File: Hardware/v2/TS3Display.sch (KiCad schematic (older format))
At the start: 28 parts, among them J1 Conn_01x05, J2 Conn_ARM_JTAG_SWD_10, SW1 SW_Push, U1 SPX3819M5-L-3-3, U2 USBLC6-2P6, U3 ATSAMD21G18A-AU, U4 NHD-2.8-240320AF-CSXP-F, U5 PAM2804, Y1 32.768k

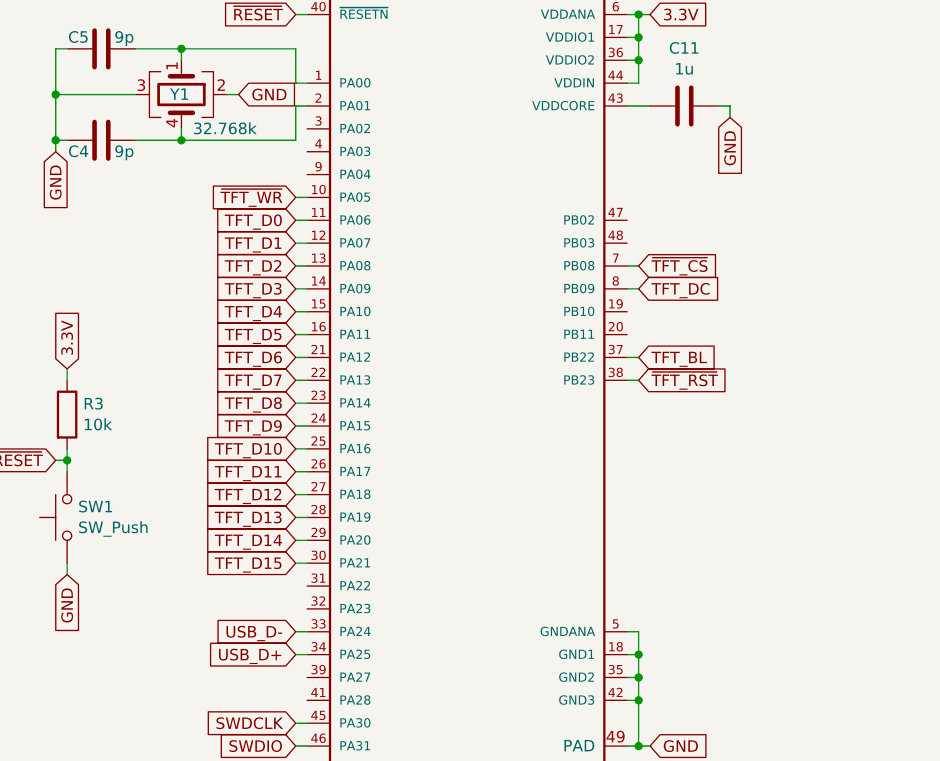
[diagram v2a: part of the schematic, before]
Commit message: Fix mirrored LCD FPC pinout
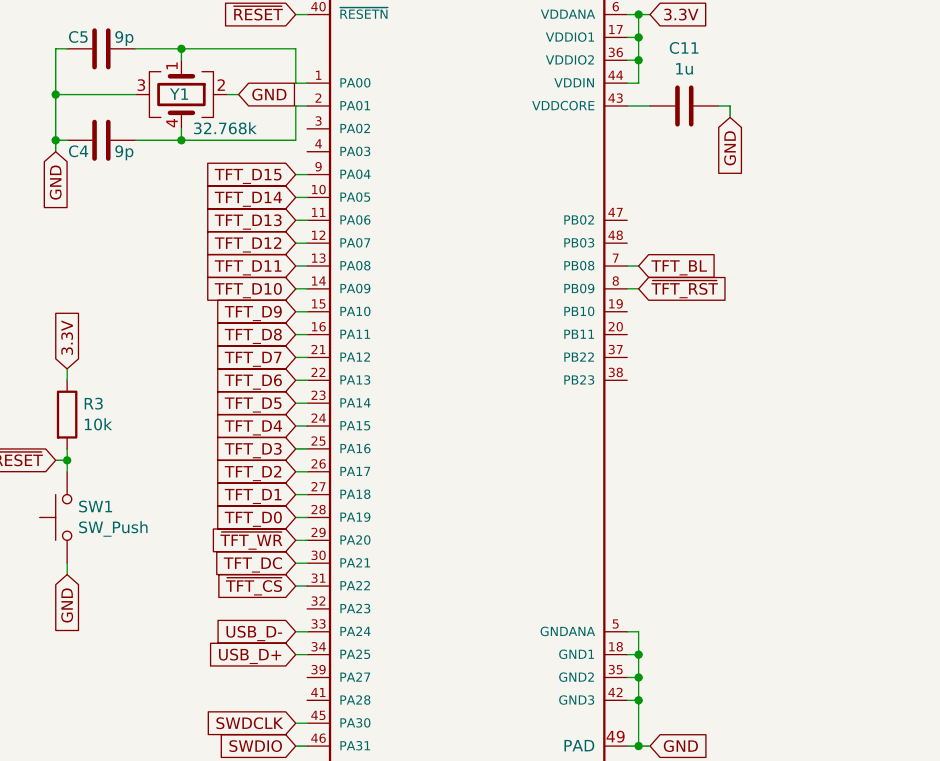
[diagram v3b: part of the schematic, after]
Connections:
- net TFT_BL: now also U3.7 (PB08); no longer U3.37 (PB22)
- net TFT_D0: now also U3.28 (PA19); no longer U3.11 (PA06)
- net TFT_D1: now also U3.27 (PA18); no longer U3.12 (PA07)
- net TFT_D10: now also U3.14 (PA09); no longer U3.25 (PA16)
- net TFT_D11: now also U3.13 (PA08); no longer U3.26 (PA17)
- net TFT_D12: now also U3.12 (PA07); no longer U3.27 (PA18)
- net TFT_D13: now also U3.11 (PA06); no longer U3.28 (PA19)
- net TFT_D14: now also U3.10 (PA05); no longer U3.29 (PA20)
- net TFT_D15: now also U3.9 (PA04); no longer U3.30 (PA21)
- net TFT_D2: now also U3.26 (PA17); no longer U3.13 (PA08)
- net TFT_D3: now also U3.25 (PA16); no longer U3.14 (PA09)
- net TFT_D4: now also U3.24 (PA15); no longer U3.15 (PA10)
- net TFT_D5: now also U3.23 (PA14); no longer U3.16 (PA11)
- net TFT_D6: now also U3.22 (PA13); no longer U3.21 (PA12)
- net TFT_D7: now also U3.21 (PA12); no longer U3.22 (PA13)
- net TFT_D8: now also U3.16 (PA11); no longer U3.23 (PA14)
- net TFT_D9: now also U3.15 (PA10); no longer U3.24 (PA15)
- net TFT_DC: now also U3.30 (PA21); no longer U3.8 (PB09)
- net ~TFT_CS: now also U3.31 (PA22); no longer U3.7 (PB08)
- net ~TFT_RST: now also U3.8 (PB09); no longer U3.38 (PB23)
- net ~TFT_WR: now also U3.29 (PA20); no longer U3.10 (PA05)
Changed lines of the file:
@@
 Wire Wire Line
 	4600 4550 4650 4550
-Wire Wire Line
-	4600 4650 4650 4650
-Wire Wire Line
-	4600 4750 4650 4750
-Text GLabel 4600 3150 0    50   Input ~ 0
-~TFT_WR
-Text GLabel 6100 3550 2    50   Input ~ 0
-TFT_DC
-Text GLabel 6100 3450 2    50   Input ~ 0
-~TFT_CS
-Text GLabel 6100 3950 2    50   Input ~ 0
-~TFT_RST
 Text GLabel 4600 5050 0    50   Input ~ 0
 USB_D-
@@
 Wire Wire Line
 	4600 5150 4650 5150
-Wire Wire Line
-	6100 3950 6050 3950
-Wire Wire Line
-	6100 3450 6050 3450
 Wire Wire Line
 	6100 3550 6050 3550
@@
 	6100 5350 6050 5350
 Connection ~ 6100 5250
-Text GLabel 6100 3850 2    50   Input ~ 0
-TFT_BL
-Wire Wire Line
-	6050 3850 6100 3850
 Wire Wire Line
 	4600 2750 4650 2750
@@
 Text GLabel 2500 2650 2    50   Input ~ 0
 3.3V
-Text GLabel 4600 3250 0    50   Input ~ 0
-TFT_D0
-Text GLabel 4600 3350 0    50   Input ~ 0
-TFT_D1
-Text GLabel 4600 3450 0    50   Input ~ 0
-TFT_D2
-Text GLabel 4600 3550 0    50   Input ~ 0
-TFT_D3
-Text GLabel 4600 3650 0    50   Input ~ 0
-TFT_D4
-Text GLabel 4600 3750 0    50   Input ~ 0
-TFT_D5
-Text GLabel 4600 3850 0    50   Input ~ 0
-TFT_D6
-Text GLabel 4600 3950 0    50   Input ~ 0
-TFT_D7
-Text GLabel 4600 4050 0    50   Input ~ 0
-TFT_D8
-Text GLabel 4600 4150 0    50   Input ~ 0
-TFT_D9
-Text GLabel 4600 4250 0    50   Input ~ 0
-TFT_D10
-Text GLabel 4600 4350 0    50   Input ~ 0
-TFT_D11
-Text GLabel 4600 4450 0    50   Input ~ 0
-TFT_D12
-Text GLabel 4600 4550 0    50   Input ~ 0
-TFT_D13
-Text GLabel 4600 4650 0    50   Input ~ 0
-TFT_D14
-Text GLabel 4600 4750 0    50   Input ~ 0
-TFT_D15
 Text GLabel 10300 1750 2    50   Input ~ 0
 TFT_D0
@@
 Wire Wire Line
 	4300 2700 4350 2700
+Text GLabel 6100 3550 2    50   Input ~ 0
+~TFT_RST
+Text GLabel 4600 4550 0    50   Input ~ 0
+TFT_D0
+Text GLabel 4600 4450 0    50   Input ~ 0
+TFT_D1
+Text GLabel 4600 4350 0    50   Input ~ 0
+TFT_D2
+Text GLabel 4600 4250 0    50   Input ~ 0
+TFT_D3
+Text GLabel 4600 4150 0    50   Input ~ 0
+TFT_D4
+Text GLabel 4600 4050 0    50   Input ~ 0
+TFT_D5
+Text GLabel 4600 3950 0    50   Input ~ 0
+TFT_D6
+Text GLabel 4600 3850 0    50   Input ~ 0
+TFT_D7
+Text GLabel 4600 3750 0    50   Input ~ 0
+TFT_D8
+Text GLabel 4600 3650 0    50   Input ~ 0
+TFT_D9
+Text GLabel 4600 3550 0    50   Input ~ 0
+TFT_D10
+Text GLabel 4600 3450 0    50   Input ~ 0
+TFT_D11
+Text GLabel 4600 3350 0    50   Input ~ 0
+TFT_D12
+Text GLabel 4600 3250 0    50   Input ~ 0
+TFT_D13
+Text GLabel 4600 3150 0    50   Input ~ 0
+TFT_D14
+Text GLabel 4600 3050 0    50   Input ~ 0
+TFT_D15
+Wire Wire Line
+	4600 3050 4650 3050
+Text GLabel 4600 4650 0    50   Input ~ 0
+~TFT_WR
+Wire Wire Line
+	4600 4650 4650 4650
+Wire Wire Line
+	6100 3450 6050 3450
+Text GLabel 6100 3450 2    50   Input ~ 0
+TFT_BL
+Text GLabel 4600 4750 0    50   Input ~ 0
+TFT_DC
+Text GLabel 4600 4850 0    50   Input ~ 0
+~TFT_CS
+Wire Wire Line
+	4600 4750 4650 4750
+Wire Wire Line
+	4600 4850 4650 4850
 $EndSCHEMATC

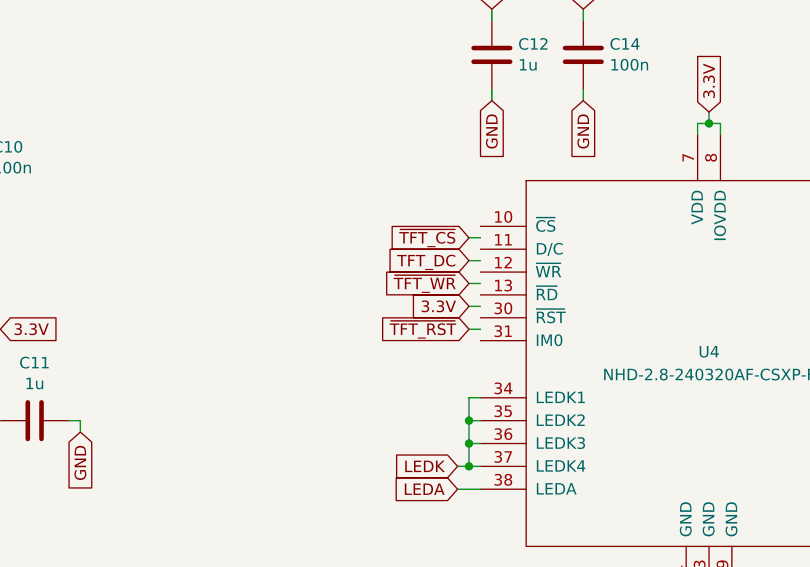
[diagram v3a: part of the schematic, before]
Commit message: Add missing IM0 pin to display and tie to ground, fixes display not initializing
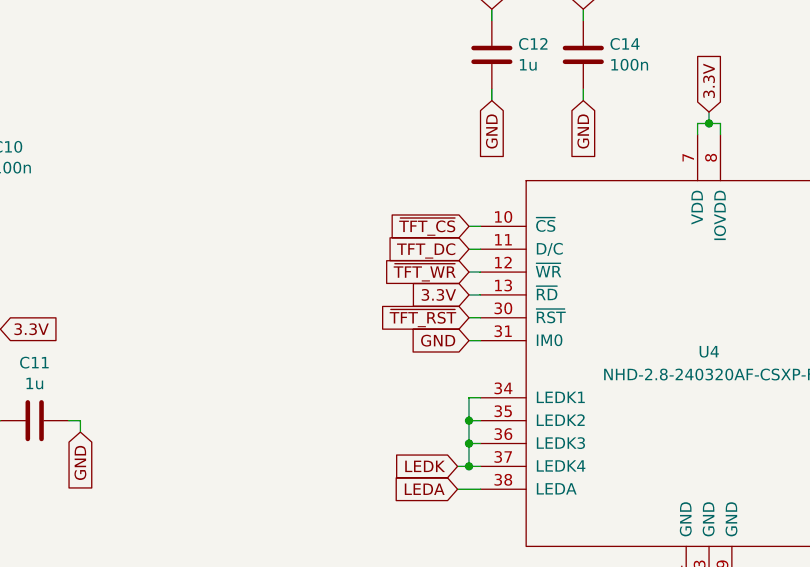
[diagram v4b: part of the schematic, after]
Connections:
- net 3.3V: now also U4.13 (~RD)
- net GND: now also U4.31 (IM0)
- net TFT_DC: now also U4.11 (D/C)
- net ~TFT_CS: now also U4.10 (~CS)
- net ~TFT_RST: now also U4.30 (~RST)
- net ~TFT_WR: now also U4.12 (~WR)
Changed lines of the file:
@@
 Wire Wire Line
 	9250 3600 9250 3550
-Text GLabel 8200 1950 0    50   Input ~ 0
+Text GLabel 8200 1900 0    50   Input ~ 0
 ~TFT_CS
-Text GLabel 8200 2050 0    50   Input ~ 0
+Text GLabel 8200 2000 0    50   Input ~ 0
 TFT_DC
-Text GLabel 8200 2350 0    50   Input ~ 0
+Text GLabel 8200 2300 0    50   Input ~ 0
 ~TFT_RST
-Text GLabel 8200 2150 0    50   Input ~ 0
+Text GLabel 8200 2100 0    50   Input ~ 0
 ~TFT_WR
-Text GLabel 8200 2250 0    50   Input ~ 0
-3.3V
-Wire Wire Line
-	8200 1950 8250 1950
-Wire Wire Line
-	8200 2050 8250 2050
-Wire Wire Line
-	8200 2150 8250 2150
-Wire Wire Line
-	8200 2250 8250 2250
-Wire Wire Line
-	8200 2350 8250 2350
+Text GLabel 8200 2200 0    50   Input ~ 0
+3.3V
+Wire Wire Line
+	8200 1900 8250 1900
+Wire Wire Line
+	8200 2000 8250 2000
+Wire Wire Line
+	8200 2100 8250 2100
+Wire Wire Line
+	8200 2200 8250 2200
+Wire Wire Line
+	8200 2300 8250 2300
 Connection ~ 9250 1450
 Wire Wire Line
@@
 Wire Wire Line
 	4600 4850 4650 4850
+Text GLabel 8200 2400 0    50   Input ~ 0
+GND
+Wire Wire Line
+	8200 2400 8250 2400
 $EndSCHEMATC
